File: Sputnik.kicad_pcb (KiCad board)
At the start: 4 copper layers, 130 x 60 mm, 132 parts, among them IC1 EP4CE10F17, J1 Pinheader_2x5_TH_WALL, U1 SN74LVC2T45, U10 SN74LVC8T245, U11 SN74LVC8T245, U12 SN74LVC8T245, U13 SN74LVC8T245, U14 SN74LVC8T245, U15 SN74LVC8T245, U16 SN74LVC2T45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

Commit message: More tuning
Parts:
- moved C86 0.40 mm to (188.2, 32.0)
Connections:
- IC1 pad A11: /RAM/A8 -> /RAM/A11
- IC1 pad B10: /RAM/A11 -> /RAM/A8
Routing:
- net /RAM/A8: track 3.51 -> 17.2 mm
- net /RAM/A6: track 4.10 -> 17.2 mm
- net /RAM/A11: track 4.43 -> 17.2 mm
- net /RAM/DQ5: track 11.1 -> 17.2 mm
- net /RAM/DQ2: track 11.9 -> 17.2 mm
- net /RAM/DQ7: track 12.1 -> 17.2 mm
- net /RAM/DQ13: track 14.6 -> 18.6 mm
- net /RAM/A4: track 17.8 -> 14.1 mm
- net /RAM/DQ0: track 13.6 -> 17.2 mm
- net /RAM/A0: track 17.9 -> 14.5 mm
- net +1V8: track 27.8 -> 27.0 mm
- net GND: track 199.0 -> 198.2 mm
- net /RAM/DQ10: track 16.7 -> 17.2 mm

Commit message: Up
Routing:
- net /RAM/LDQS: track 11.1 -> 17.2 mm
- net /RAM/LDM: track 12.7 -> 18.7 mm
- net /RAM/DQ7: track 17.2 -> 13.4 mm
- net GND: track 198.2 -> 198.9 mm
- net +1V8: track 27.0 -> 27.7 mm
- net /RAM/DQ8: track 17.8 -> 17.2 mm

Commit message: Up..
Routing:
- net /RAM/LDM: track 18.7 -> 23.7 mm
- net /RAM/UDM: track 14.5 -> 17.2 mm
- net /RAM/UDQS: track 15.2 -> 17.1 mm

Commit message: More tuning...
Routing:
- net (no net): track 16.7 -> 0.00 mm
- net /RAM/LDM: track 23.7 -> 17.2 mm
- net /RAM/A4: track 14.1 -> 17.9 mm
- net /RAM/DQ7: track 13.4 -> 17.2 mm
- net /RAM/A0: track 14.5 -> 17.9 mm

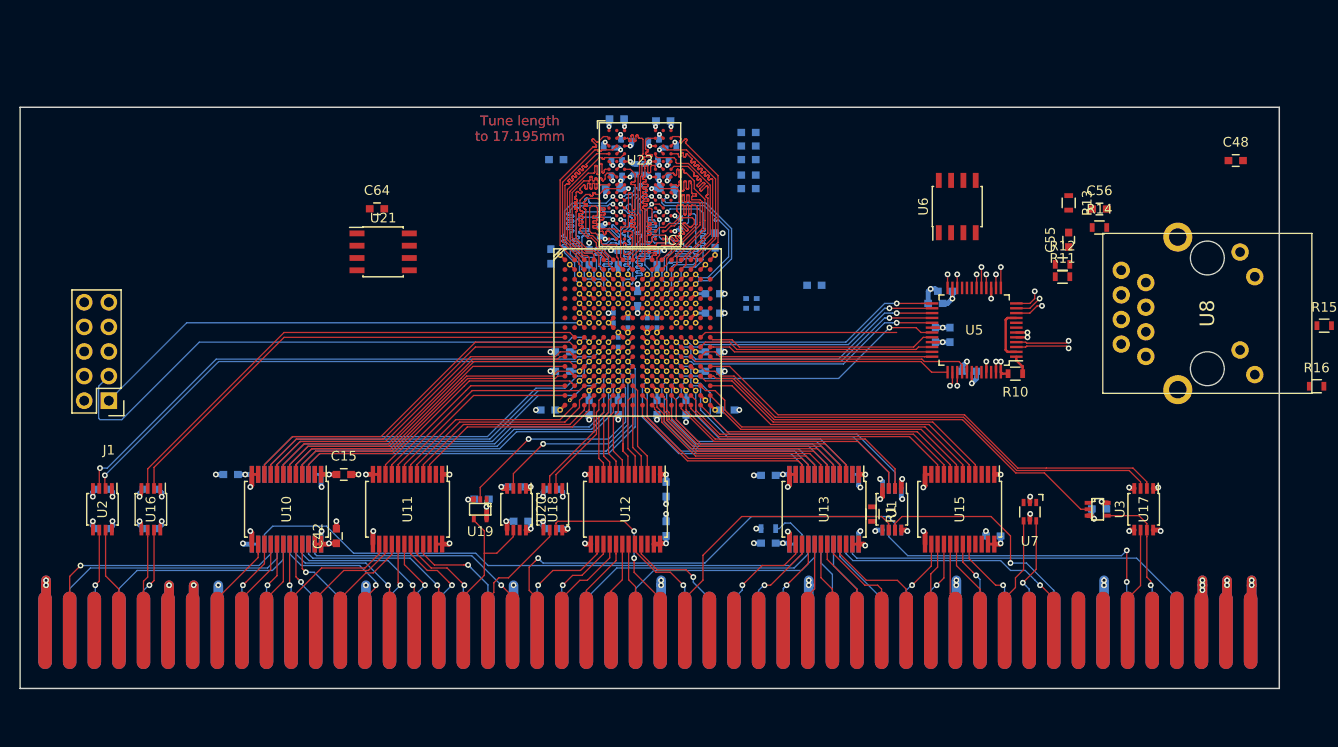
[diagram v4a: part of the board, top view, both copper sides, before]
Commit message: 1V8 caps added, bit of routing
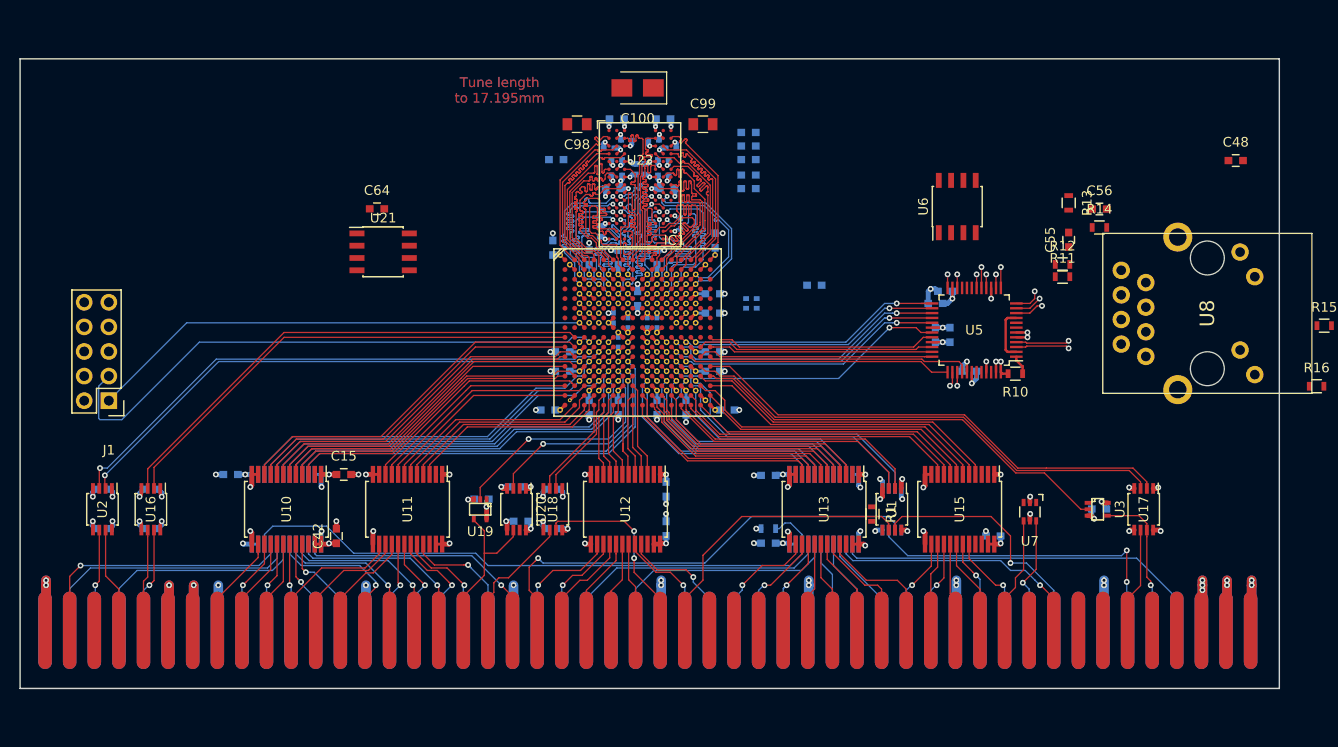
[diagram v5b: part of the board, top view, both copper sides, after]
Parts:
- added C100: 47uF, Capacitors_Tantalum_SMD:CP_Tantalum_Case-B_EIA-3528-21_Wave, F.Cu at (183.8, 18.0)
- added C98: 10uF, Capacitors_SMD:C_0805, F.Cu at (177.5, 21.8)
- added C99: 10uF, Capacitors_SMD:C_0805, F.Cu at (190.5, 21.8)
- moved C81 0.92 mm to (175.0, 34.5), turned to 90 degrees
- moved C76 0.20 mm to (186.4, 21.2)
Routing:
- net Net-(IC1-PadJ15): track 20.5 -> 0.00 mm
- net GND: track 198.9 -> 199.7 mm, vias 96 -> 97
- net +1V8: track 27.7 -> 28.4 mm
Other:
- board size 130 x 60 mm -> 130 x 65 mm

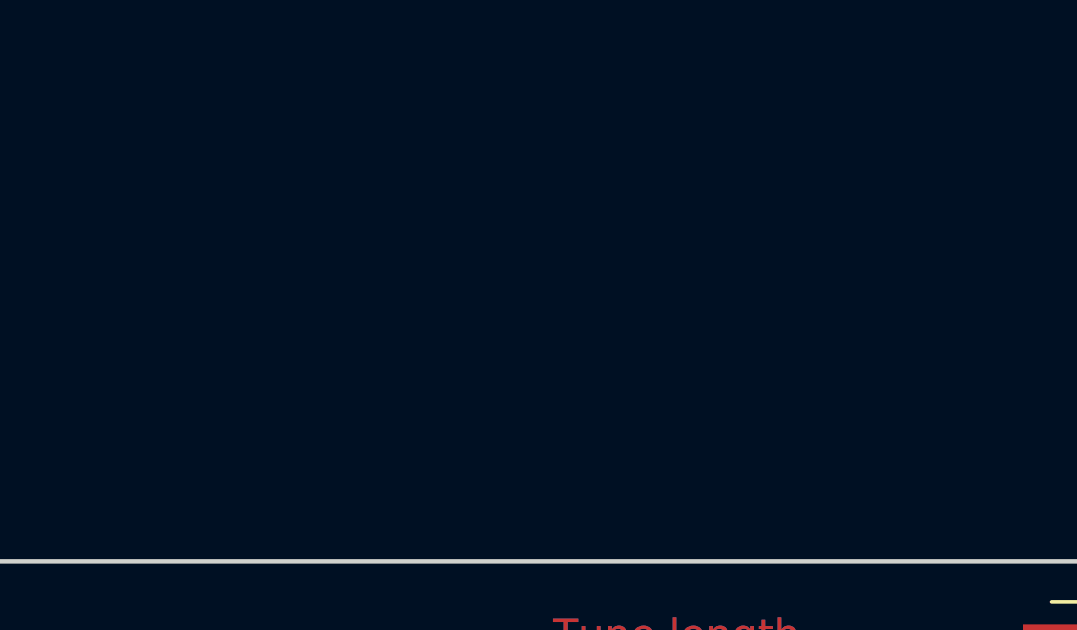
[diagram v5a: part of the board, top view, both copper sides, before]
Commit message: Added power sheet, 1V8 chip docs etc
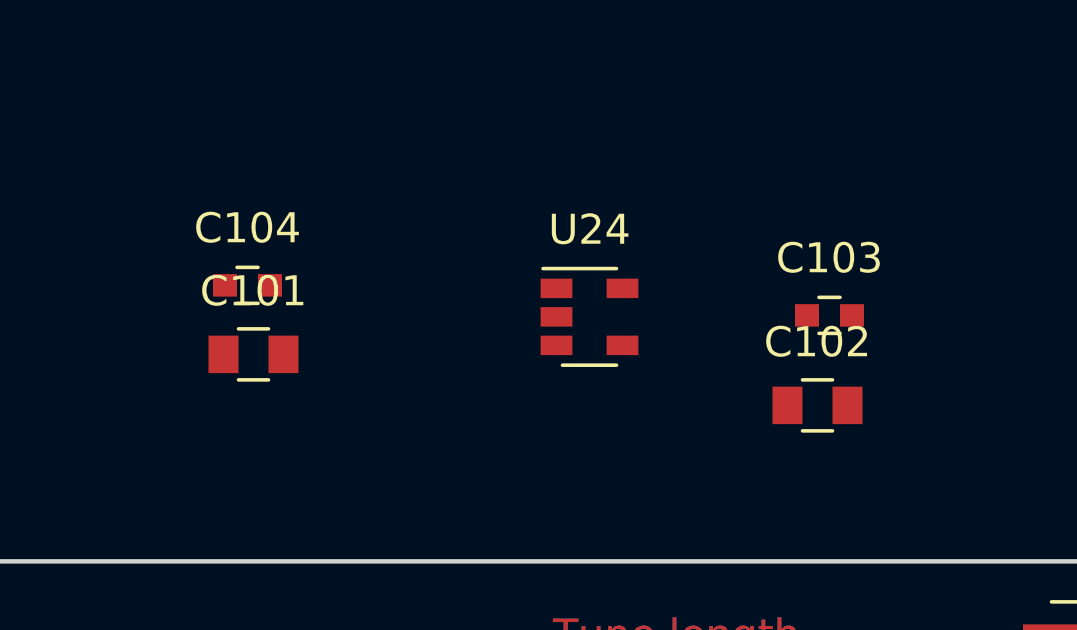
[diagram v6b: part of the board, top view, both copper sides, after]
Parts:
- added C101: 4,7uF, Capacitors_SMD:C_0805, F.Cu at (155.4, 8.10)
- added C102: 4,7uF, Capacitors_SMD:C_0805, F.Cu at (174.2, 9.80)
- added C103: DNP, Capacitors_SMD:C_0603, F.Cu at (174.6, 6.80)
- added C104: 0,1, Capacitors_SMD:C_0603, F.Cu at (155.2, 5.80)
- added U24: TLV62569P, TO_SOT_Packages_SMD:SOT-23-5, F.Cu at (166.6, 6.85)
- R2: value TBD -> 200K
- R3: value TBD -> 100K
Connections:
- net /RAM/ODT renamed Net-(U22-PadK9)
- R2 pad 1: Net-(R2-Pad1) -> +1V8
- R2 pad 2: GND -> Net-(C103-Pad2)
- R3 pad 1: Net-(R3-Pad1) -> Net-(C103-Pad2)

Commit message: More 1V8 stuff
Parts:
- added L1: SRN6045-2R2Y, zorro:SRN6045, F.Cu at (166.5, 26.3)
- C102: value 4,7uF -> 10uF
- moved R2 197.2 mm to (165.2, 37.1), turned to 180 degrees
- moved R3 193.9 mm to (165.2, 35.2)
- moved C104 26.7 mm to (160.2, 32.0), turned to 270 degrees
- moved U24 25.7 mm to (165.5, 32.5), turned to 180 degrees
- moved C103 25.6 mm to (170.3, 32.0), turned to 270 degrees
- moved C101 24.8 mm to (162.1, 32.0), turned to 270 degrees
- moved C102 23.0 mm to (168.4, 32.0), turned to 270 degrees
- moved U21 6.63 mm to (151.1, 36.8)
- moved C64 6.02 mm to (151.1, 32.4)
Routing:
- net Net-(C103-Pad2): track 0.00 -> 3.68 mm
- added copper zone on F.Cu, net +1V8
- added copper zone on F.Cu, net GND

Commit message: Update 1V8 PSU
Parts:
- moved C103 6.94 mm to (165.2, 36.8), turned to 180 degrees
- moved C74 2.57 mm to (177.5, 24.0)
- moved R3 2.25 mm to (163.0, 35.2), turned to 180 degrees
- moved L1 1.88 mm to (168.4, 26.3)
- moved R2 1.85 mm to (165.2, 35.2)
- moved C104 0.84 mm to (161.0, 32.0)
- moved C101 0.53 mm to (162.6, 32.0)
- moved C102 0.38 mm to (168.8, 32.0)
- moved U24 0.12 mm to (165.5, 32.4)
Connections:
- net Net-(C103-Pad2) renamed /Power/FB1V8
- net Net-(L1-Pad1) renamed /Power/SW1V8
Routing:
- net +5VDC: track 32.2 -> 115.2 mm, vias 16 -> 19
- net +1V8: track 28.4 -> 58.6 mm, vias 16 -> 36
- net GND: track 199.7 -> 227.2 mm, vias 97 -> 113
- net /Power/SW1V8: track 0.00 -> 3.63 mm, vias 0 -> 3
- net /Power/FB1V8: track 3.68 -> 5.92 mm
- added copper zone on F.Cu, net +5VDC
- added copper zone on F.Cu, net /Power/SW1V8
